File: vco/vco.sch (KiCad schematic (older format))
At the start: 53 parts

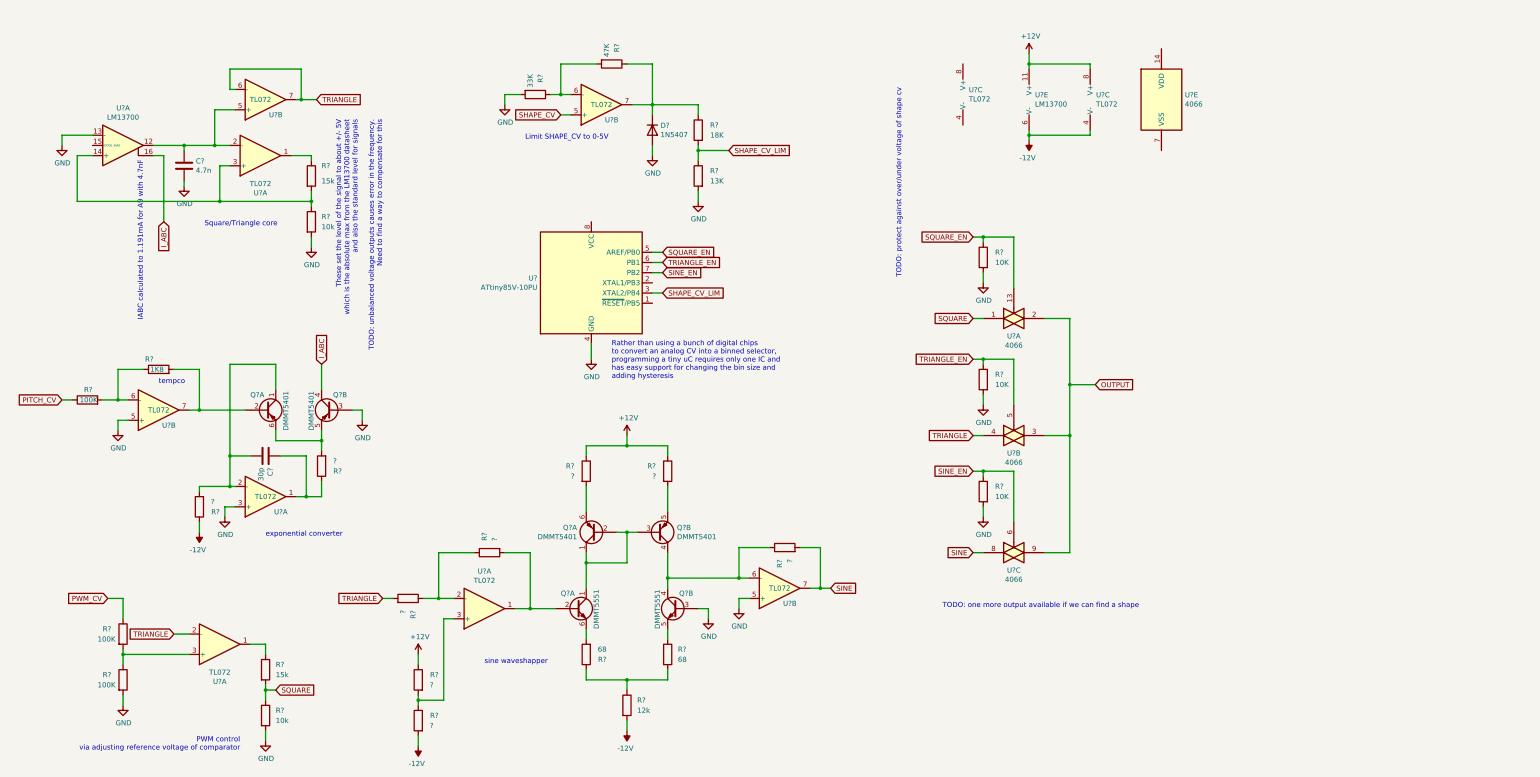
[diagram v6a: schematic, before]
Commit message: vco adjustments
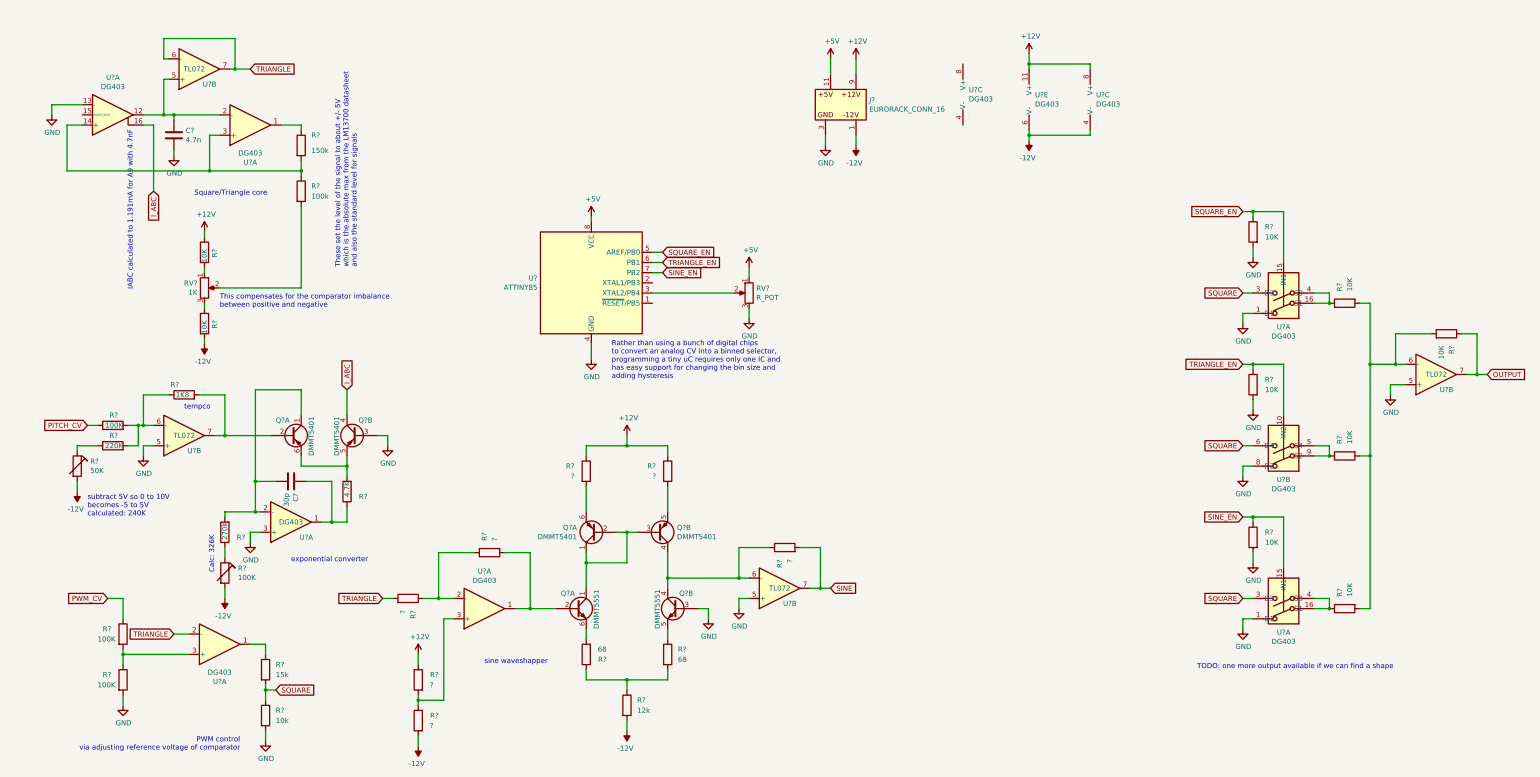
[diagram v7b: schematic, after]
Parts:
- removed D?: 1N5407, Diode_THT:D_DO-201AD_P15.24mm_Horizontal, symbol Diode:1N5407
- removed R? (x2): 10K, symbol Device:R
- removed R?: 47K, symbol Device:R
- removed R?: 33K, symbol Device:R
- removed R?: 13K, symbol Device:R
- removed R?: 18K, symbol Device:R
- removed U? (x4): 4066, symbol 4xxx:4066
- removed U?: TL072, symbol Amplifier_Operational:TL072
- added J?: EURORACK_CONN_16, synth:EURORACK_16_IDC, symbol synth:EURORACK_CONN_16
- added R? (x8): 10K, symbol Device:R
- added R?: 220K, symbol Device:R
- added R?: 50K, symbol Device:RTRIM
- added R?: 100K, symbol Device:RTRIM
- added RV?: 1K, symbol Device:R_POT
- added RV?: R_POT, symbol Device:R_POT
- added U? (x3): DG403, Package_SO:SOIC-16_3.9x9.9mm_P1.27mm, symbol synth:DG403
- added U?: TL072, symbol Amplifier_Operational:TL072
- R?: value ? -> 4.7K
- R?: value ? -> 270K
- R?: value 15k -> 150k
- R?: value 10k -> 100k
- U? (x2): value LM13700 -> DG403; footprint (none) -> Package_SO:SOIC-16_3.9x9.9mm_P1.27mm
- U? (x6): value TL072 -> DG403; footprint (none) -> Package_SO:SOIC-16_3.9x9.9mm_P1.27mm
- U?: value ATtiny85V-10PU -> ATTINY85; footprint Package_DIP:DIP-8_W7.62mm -> Package_SO:SOIC-16_3.9x9.9mm_P1.27mm
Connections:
- net +12V: now also J?.9 (12V_P), R?.1
- net -12V: now also J?.1 (12V_N), R?.2, R?.2, R?.2; no longer R?.1
- net GND: now also J?.3 (GND), R?.2, R?.2, RV?.3, U?.1 (D1), U?.1 (D1), U?.5 (+), U?.8 (D2); no longer R?.2
- net OUTPUT: now also R?.1, U?.7
- net SINE_EN: now also R?.1, U?.15 (IN1)
- net SQUARE: now also U?.3 (D3), U?.3 (D3), U?.6 (D4)
- net SQUARE_EN: now also U?.15 (IN1)
- net TRIANGLE_EN: now also R?.1, U?.10 (IN2)
- net at R?.1, R?.2, U?.6 (-): now also R?.2
- net +5V: now reaches U?.8 (VCC)
- net +5V: now also J?.11 (5V), RV?.1
- net SHAPE_CV_LIM: no longer names the net of U?.3 (XTAL2/PB4)
- net SHAPE_CV_LIM: now also RV?.2
- new net: R?.1, R?.1 (x2)
- new net: R?.2, RV?.2
- new net: R?.2, RV?.1
- new net: R?.1, RV?.3
- new net: R?.1, U?.16 (S1), U?.4 (S3) (x2)
- new net: R?.2, R?.2, R?.2, R?.2, U?.6 (-)
- new net: R?.1, U?.5 (S4), U?.9 (S2)
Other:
- note added: "Calc: 326K"
- note added: "These set the level of the signal to about +/- 5V\nwhich is the absolute max from the LM13700 datasheet\nand also the standard level for signals"
- note added: "This compensates for the comparator imbalance\nbetween positive and negative"
- note added: "subtract 5V so 0 to 10V\nbecomes -5 to 5V\ncalculated: 240K"
- note removed: "Limit SHAPE_CV to 0-5V"
- note removed: "TODO: protect against over/under voltage of shape cv"
- note removed: "These set the level of the signal to about +/- 5V\nwhich is the absolute max from the LM13700 datasheet\nand also the standard level for signals\n\nTODO: unbalanced voltage outputs causes error in the frequency.\nNeed to find a way to compensate for this"
- moved on the sheet: C?, Q?A, Q?B, R?, U?A, U?B

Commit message: assembled breadboard VCO and waveshaper
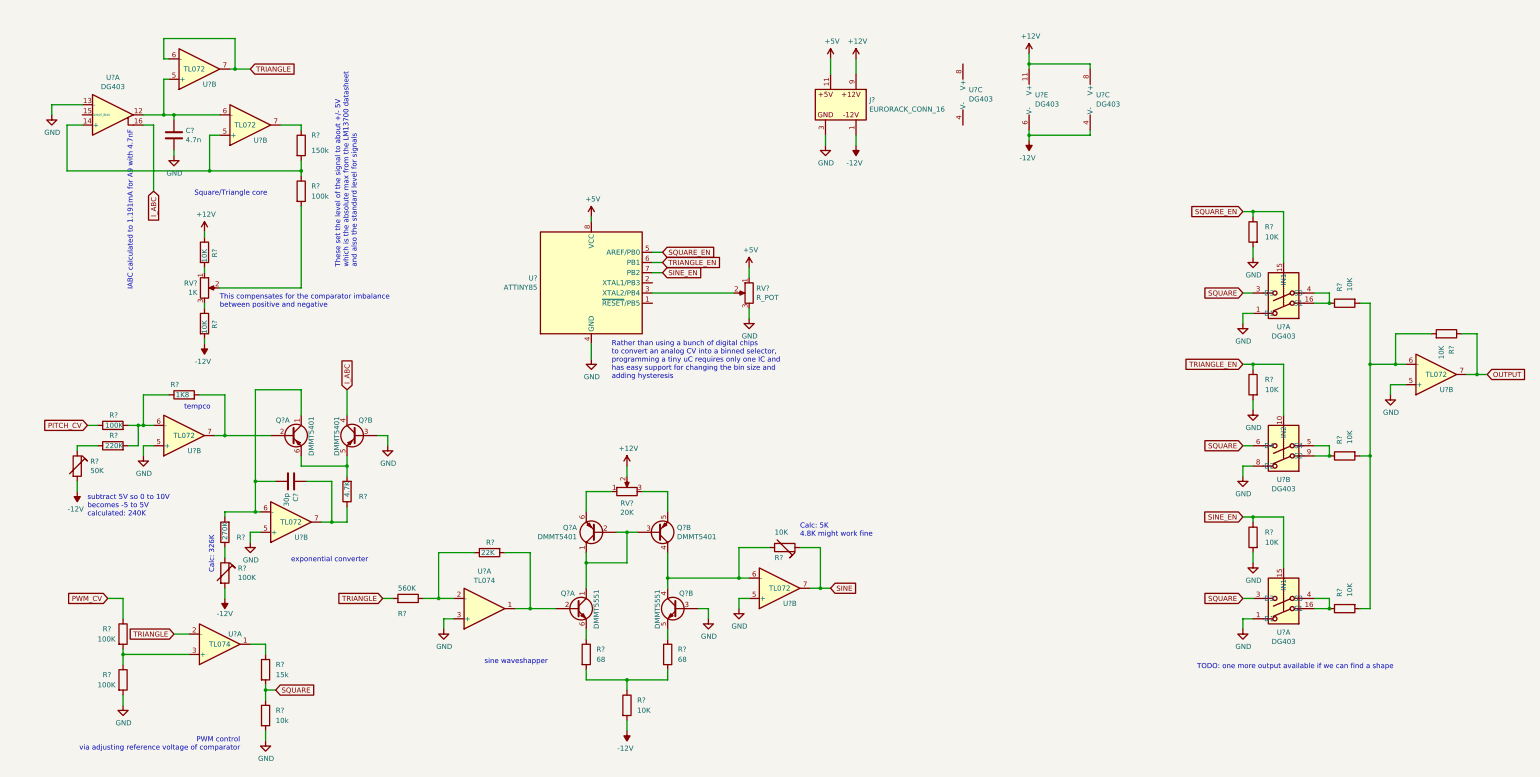
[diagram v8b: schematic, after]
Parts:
- removed R? (x6): ?, symbol Device:R
- removed R?: 68, symbol Device:R
- removed U? (x4): DG403, Package_SO:SOIC-16_3.9x9.9mm_P1.27mm, symbol Amplifier_Operational:TL072
- added R?: 68, symbol Device:R
- added R?: 10K, symbol Device:RTRIM
- added R?: 560K, symbol Device:R
- added RV?: 20K, symbol Device:R_POT
- added U? (x2): TL074, symbol Amplifier_Operational:TL074
- added U? (x2): TL072, symbol Amplifier_Operational:TL072
- R?: value 12k -> 10K
- R?: value ? -> 22K
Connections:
- net +12V: now also RV?.2
- net GND: now also U?.3 (+), U?.5 (+)
- net SINE: now also R?.1
- net TRIANGLE: now also R?.2, U?.2 (-)
- net at C?.1, U?.12, U?.5 (+): now also U?.6 (-)
- net at R?.1, R?.2, U?.14 (+): now also U?.5 (+)
- net at R?.1: now also U?.7
- net at C?.2, Q?.1 (C1), R?.2: now also U?.6 (-)
- net at C?.1, R?.1: now also U?.7
- net at Q?.2 (B1), R?.2: now also U?.1
- net at Q?.6 (E1): now also R?.1
- net at Q?.4 (C2), Q?.4 (C2), U?.6 (-): now also R?.2
- net at R?.1, R?.2: now also R?.2
- net at Q?.6 (E1): now also RV?.1
- net at Q?.5 (E2): now also RV?.3
- net at R?.1: now also R?.1, U?.2 (-)
- net at R?.1: now also U?.1
- net at R?.1, R?.2: now also U?.3 (+)
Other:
- note added: "Calc: 5K\n4.8K might work fine"
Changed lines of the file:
@@
-$Comp
-L Amplifier_Operational:TL072 U?
-U 1 1 5EC71D01
-P 2550 1350
-F 0 "U?" H 2550 1717 50  0000 C CNN
-F 1 "DG403" H 2550 1626 50  0000 C CNN
-F 2 "Package_SO:SOIC-16_3.9x9.9mm_P1.27mm" H 2550 1350 50  0001 C CNN
-F 3 "https://www.renesas.com/us/en/www/doc/datasheet/dg401-03.pdf" H 2550 1350 50  0001 C CNN
-	1    2550 1350
-	1    0    0    1
-$EndComp
 $Comp
 L Amplifier_Operational:TL072 U?
@@
 $EndComp
 $Comp
-L Amplifier_Operational:TL072 U?
-U 1 1 5ECBF24F
-P 2950 5250
-F 0 "U?" H 3100 5400 50  0000 C CNN
-F 1 "DG403" H 2950 5250 50  0000 C CNN
-F 2 "Package_SO:SOIC-16_3.9x9.9mm_P1.27mm" H 2950 5250 50  0001 C CNN
-F 3 "https://www.renesas.com/us/en/www/doc/datasheet/dg401-03.pdf" H 2950 5250 50  0001 C CNN
-	1    2950 5250
-	1    0    0    1
-$EndComp
-$Comp
 L Device:R R?
 U 1 1 5ECC5F0B
@@
 P 6250 7050
 F 0 "R?" H 6350 7100 50  0000 L CNN
-F 1 "12k" H 6350 7000 50  0000 L CNN
+F 1 "10K" H 6350 7000 50  0000 L CNN
 F 2 "" V 6180 7050 50  0001 C CNN
 F 3 "~" H 6250 7050 50  0001 C CNN
@@
 Text GLabel 2800 6900 2    50   Input ~ 0
 SQUARE
-$Comp
-L Device:R R?
-U 1 1 5ED26FEA
-P 5850 4750
-F 0 "R?" H 5650 4800 50  0000 L CNN
-F 1 "?" H 5700 4700 50  0000 L CNN
-F 2 "" V 5780 4750 50  0001 C CNN
-F 3 "~" H 5850 4750 50  0001 C CNN
-	1    5850 4750
-	1    0    0    -1
-$EndComp
-$Comp
-L Device:R R?
-U 1 1 5ED27954
-P 6650 4750
-F 0 "R?" H 6450 4800 50  0000 L CNN
-F 1 "?" H 6500 4700 50  0000 L CNN
-F 2 "" V 6580 4750 50  0001 C CNN
-F 3 "~" H 6650 4750 50  0001 C CNN
-	1    6650 4750
-	1    0    0    -1
-$EndComp
 $Comp
 L power:+12V #PWR?
@@
 $EndComp
 $Comp
-L Device:R R?
-U 1 1 5ED4E809
-P 4200 6800
-F 0 "R?" H 4000 6850 50  0000 L CNN
-F 1 "?" H 4050 6750 50  0000 L CNN
-F 2 "" V 4130 6800 50  0001 C CNN
-F 3 "~" H 4200 6800 50  0001 C CNN
-	1    4200 6800
-	-1   0    0    -1
-$EndComp
-$Comp
-L Device:R R?
-U 1 1 5ED58116
-P 4200 7200
-F 0 "R?" H 4000 7250 50  0000 L CNN
-F 1 "?" H 4050 7150 50  0000 L CNN
-F 2 "" V 4130 7200 50  0001 C CNN
-F 3 "~" H 4200 7200 50  0001 C CNN
-	1    4200 7200
-	-1   0    0    -1
-$EndComp
-$Comp
 L power:-12V #PWR?
 U 1 1 5ECF6305
 P 2300 6000
 F 0 "#PWR?" H 2300 6100 50  0001 C CNN
-F 1 "-12V" H 2315 6173 50  0000 C CNN
+F 1 "-12V" H 2300 6150 50  0000 C CNN
 F 2 "" H 2300 6000 50  0001 C CNN
 F 3 "" H 2300 6000 50  0001 C CNN
@@
 L power:+12V #PWR?
 U 1 1 5ED7F3FD
-P 6250 4400
-F 0 "#PWR?" H 6250 4250 50  0001 C CNN
-F 1 "+12V" H 6265 4573 50  0000 C CNN
-F 2 "" H 6250 4400 50  0001 C CNN
-F 3 "" H 6250 4400 50  0001 C CNN
-	1    6250 4400
-	1    0    0    -1
-$EndComp
-$Comp
-L power:+12V #PWR?
-U 1 1 5EDA2507
-P 4200 6550
-F 0 "#PWR?" H 4200 6400 50  0001 C CNN
-F 1 "+12V" H 4215 6723 50  0000 C CNN
-F 2 "" H 4200 6550 50  0001 C CNN
-F 3 "" H 4200 6550 50  0001 C CNN
-	1    4200 6550
-	1    0    0    -1
-$EndComp
-$Comp
-L Device:R R?
-U 1 1 5EDB1330
-P 4100 6000
-F 0 "R?" H 3900 6050 50  0000 L CNN
-F 1 "?" H 3950 5950 50  0000 L CNN
-F 2 "" V 4030 6000 50  0001 C CNN
-F 3 "~" H 4100 6000 50  0001 C CNN
-	1    4100 6000
-	0    1    -1   0
+P 6250 4700
+F 0 "#PWR?" H 6250 4550 50  0001 C CNN
+F 1 "+12V" H 6265 4873 50  0000 C CNN
+F 2 "" H 6250 4700 50  0001 C CNN
+F 3 "" H 6250 4700 50  0001 C CNN
+	1    6250 4700
+	1    0    0    -1
 $EndComp
 $Comp
@@
 	1    0    0    1
 $EndComp
-Wire Wire Line
-	4200 6550 4200 6650
-Wire Wire Line
-	4200 7450 4200 7350
-Wire Wire Line
-	4200 6950 4200 7000
-$Comp
-L Device:R R?
-U 1 1 5EEC949A
-P 5850 6550
-F 0 "R?" H 5650 6600 50  0000 L CNN
-F 1 "68" H 5650 6500 50  0000 L CNN
-F 2 "" V 5780 6550 50  0001 C CNN
-F 3 "~" H 5850 6550 50  0001 C CNN
-	1    5850 6550
-	-1   0    0    1
-$EndComp
 $Comp
 L Device:R R?
@@
 	1    0    0    -1
 $EndComp
-Connection ~ 4200 7000
-Wire Wire Line
-	4200 7000 4200 7050
 $Comp
 L Amplifier_Operational:TL072 U?
@@
 	1    0    0    1
 $EndComp
-$Comp
-L Device:R R?
-U 1 1 5EF63C48
-P 7800 5500
-F 0 "R?" H 7600 5550 50  0000 L CNN
-F 1 "?" H 7650 5450 50  0000 L CNN
-F 2 "" V 7730 5500 50  0001 C CNN
-F 3 "~" H 7800 5500 50  0001 C CNN
-	1    7800 5500
-	0    -1   -1   0
-$EndComp
 Wire Wire Line
 	7350 6100 7350 6000
@@
 Connection ~ 2400 800
 $Comp
-L Amplifier_Operational:TL072 U?
-U 1 1 5EDF33EF
-P 2250 6450
-F 0 "U?" H 2250 6817 50  0000 C CNN
-F 1 "DG403" H 2250 6726 50  0000 C CNN
-F 2 "Package_SO:SOIC-16_3.9x9.9mm_P1.27mm" H 2250 6450 50  0001 C CNN
-F 3 "https://www.renesas.com/us/en/www/doc/datasheet/dg401-03.pdf" H 2250 6450 50  0001 C CNN
-	1    2250 6450
-	1    0    0    1
-$EndComp
-$Comp
 L Device:R R?
 U 1 1 5EE0590C
@@
 	2700 6900 2700 6850
 Wire Wire Line
-	6250 4400 6250 4500
-Connection ~ 6250 4500
-Wire Wire Line
 	6250 7300 6250 7200
-$Comp
-L power:-12V #PWR?
-U 1 1 5EE46E0E
-P 4200 7450
-F 0 "#PWR?" H 4200 7550 50  0001 C CNN
-F 1 "-12V" H 4215 7623 50  0000 C CNN
-F 2 "" H 4200 7450 50  0001 C CNN
-F 3 "" H 4200 7450 50  0001 C CNN
-	1    4200 7450
-	-1   0    0    1
-$EndComp
 $Comp
 L Device:R R?
 U 1 1 5EE5FE30
 P 4900 5550
-F 0 "R?" H 4700 5600 50  0000 L CNN
-F 1 "?" H 4750 5500 50  0000 L CNN
+F 0 "R?" V 4800 5500 50  0000 L CNN
+F 1 "22K" V 4900 5500 50  0000 L CNN
 F 2 "" V 4830 5550 50  0001 C CNN
 F 3 "~" H 4900 5550 50  0001 C CNN
@@
 	6650 5900 6650 5800
 Wire Wire Line
-	5850 4500 5850 4600
-Wire Wire Line
-	5850 4500 6250 4500
-Wire Wire Line
-	6650 4500 6650 4600
-Wire Wire Line
-	6250 4500 6650 4500
-Wire Wire Line
-	6650 4900 6650 5150
-Wire Wire Line
-	5850 5150 5850 4900
+	5850 5150 5850 4950
 Wire Wire Line
 	5850 5550 5850 5650
@@
 Wire Wire Line
 	3850 6000 3950 6000
-$Comp
-L Amplifier_Operational:TL072 U?
-U 1 1 5EFB5E2F
-P 4850 6100
-F 0 "U?" H 4850 5733 50  0000 C CNN
-F 1 "DG403" H 4850 5824 50  0000 C CNN
-F 2 "Package_SO:SOIC-16_3.9x9.9mm_P1.27mm" H 4850 6100 50  0001 C CNN
-F 3 "https://www.renesas.com/us/en/www/doc/datasheet/dg401-03.pdf" H 4850 6100 50  0001 C CNN
-	1    4850 6100
-	1    0    0    1
-$EndComp
 Wire Wire Line
 	4450 6200 4550 6200
@@
 Wire Wire Line
 	5300 6100 5150 6100
-Wire Wire Line
-	4250 6000 4400 6000
 Connection ~ 4400 6000
-Wire Wire Line
-	4450 6200 4450 7000
-Wire Wire Line
-	4200 7000 4450 7000
 Wire Wire Line
 	5550 6100 5300 6100
@@
 Wire Wire Line
 	5900 2300 5900 2250
+$Comp
+L Device:R R?
+U 1 1 5F5E87D1
+P 5850 6550
+F 0 "R?" H 5950 6600 50  0000 L CNN
+F 1 "68" H 5950 6500 50  0000 L CNN
+F 2 "" V 5780 6550 50  0001 C CNN
+F 3 "~" H 5850 6550 50  0001 C CNN
+	1    5850 6550
+	1    0    0    -1
+$EndComp
+$Comp
+L Amplifier_Operational:TL074 U?
+U 1 1 5F5FA713
+P 4850 6100
+F 0 "U?" H 4850 5733 50  0000 C CNN
+F 1 "TL074" H 4850 5824 50  0000 C CNN
+F 2 "" H 4800 6200 50  0001 C CNN
+F 3 "http://www.ti.com/lit/ds/symlink/tl071.pdf" H 4900 6300 50  0001 C CNN
+	1    4850 6100
+	1    0    0    1
+$EndComp
+$Comp
+L Amplifier_Operational:TL074 U?
+U 1 1 5F62E4F6
+P 2250 6450
+F 0 "U?" H 2400 6350 50  0000 C CNN
+F 1 "TL074" H 2250 6450 50  0000 C CNN
+F 2 "" H 2200 6550 50  0001 C CNN
+F 3 "http://www.ti.com/lit/ds/symlink/tl071.pdf" H 2300 6650 50  0001 C CNN
+	1    2250 6450
+	1    0    0    1
+$EndComp
+$Comp
+L Amplifier_Operational:TL072 U?
+U 2 1 5F63B234
+P 2950 5250
+F 0 "U?" H 3050 5400 50  0000 C CNN
+F 1 "TL072" H 2950 5250 50  0000 C CNN
+F 2 "" H 2950 5250 50  0001 C CNN
+F 3 "http://www.ti.com/lit/ds/symlink/tl071.pdf" H 2950 5250 50  0001 C CNN
+	2    2950 5250
+	1    0    0    1
+$EndComp
+$Comp
+L Amplifier_Operational:TL072 U?
+U 2 1 5F6493F7
+P 2550 1350
+F 0 "U?" H 2650 1500 50  0000 C CNN
+F 1 "TL072" H 2500 1350 50  0000 C CNN
+F 2 "" H 2550 1350 50  0001 C CNN
+F 3 "http://www.ti.com/lit/ds/symlink/tl071.pdf" H 2550 1350 50  0001 C CNN
+	2    2550 1350
+	1    0    0    1
+$EndComp
+$Comp
+L Device:RTRIM R?
+U 1 1 5F64E916
+P 7800 5500
+F 0 "R?" V 7900 5400 50  0000 L CNN
+F 1 "10K" V 7650 5400 50  0000 L CNN
+F 2 "" V 7730 5500 50  0001 C CNN
+F 3 "~" H 7800 5500 50  0001 C CNN
+	1    7800 5500
+	0    1    1    0
+$EndComp
+Text Notes 7950 5400 0    50   ~ 0
+Calc: 5K\n4.8K might work fine
+$Comp
+L Device:R_POT RV?
+U 1 1 5F748C59
+P 6250 4950
+F 0 "RV?" V 6135 4950 50  0000 C CNN
+F 1 "20K" V 6044 4950 50  0000 C CNN
+F 2 "" H 6250 4950 50  0001 C CNN
+F 3 "~" H 6250 4950 50  0001 C CNN
+	1    6250 4950
+	0    -1   -1   0
+$EndComp
+$Comp
+L power:GND #PWR?
+U 1 1 5F775FBE
+P 4450 6300
+F 0 "#PWR?" H 4450 6050 50  0001 C CNN
+F 1 "GND" H 4455 6127 50  0000 C CNN
+F 2 "" H 4450 6300 50  0001 C CNN
+F 3 "" H 4450 6300 50  0001 C CNN
+	1    4450 6300
+	1    0    0    -1
+$EndComp
+Wire Wire Line
+	4450 6300 4450 6200
+$Comp
+L Device:R R?
+U 1 1 5F7D4E50
+P 4100 6000
+F 0 "R?" V 3950 5900 50  0000 L CNN
+F 1 "560K" V 4200 5900 50  0000 L CNN
+F 2 "" V 4030 6000 50  0001 C CNN
+F 3 "~" H 4100 6000 50  0001 C CNN
+	1    4100 6000
+	0    1    -1   0
+$EndComp
+Wire Wire Line
+	6100 4950 5850 4950
+Wire Wire Line
+	6400 4950 6650 4950
+Wire Wire Line
+	6650 4950 6650 5150
+Wire Wire Line
+	6250 4700 6250 4800
+Wire Wire Line
+	4250 6000 4400 6000
 $EndSCHEMATC
